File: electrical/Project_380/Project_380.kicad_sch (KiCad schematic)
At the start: 6 parts, among them J14 UART_to_USB, SW1 SW_SPST, U2 ESP32-WROOM

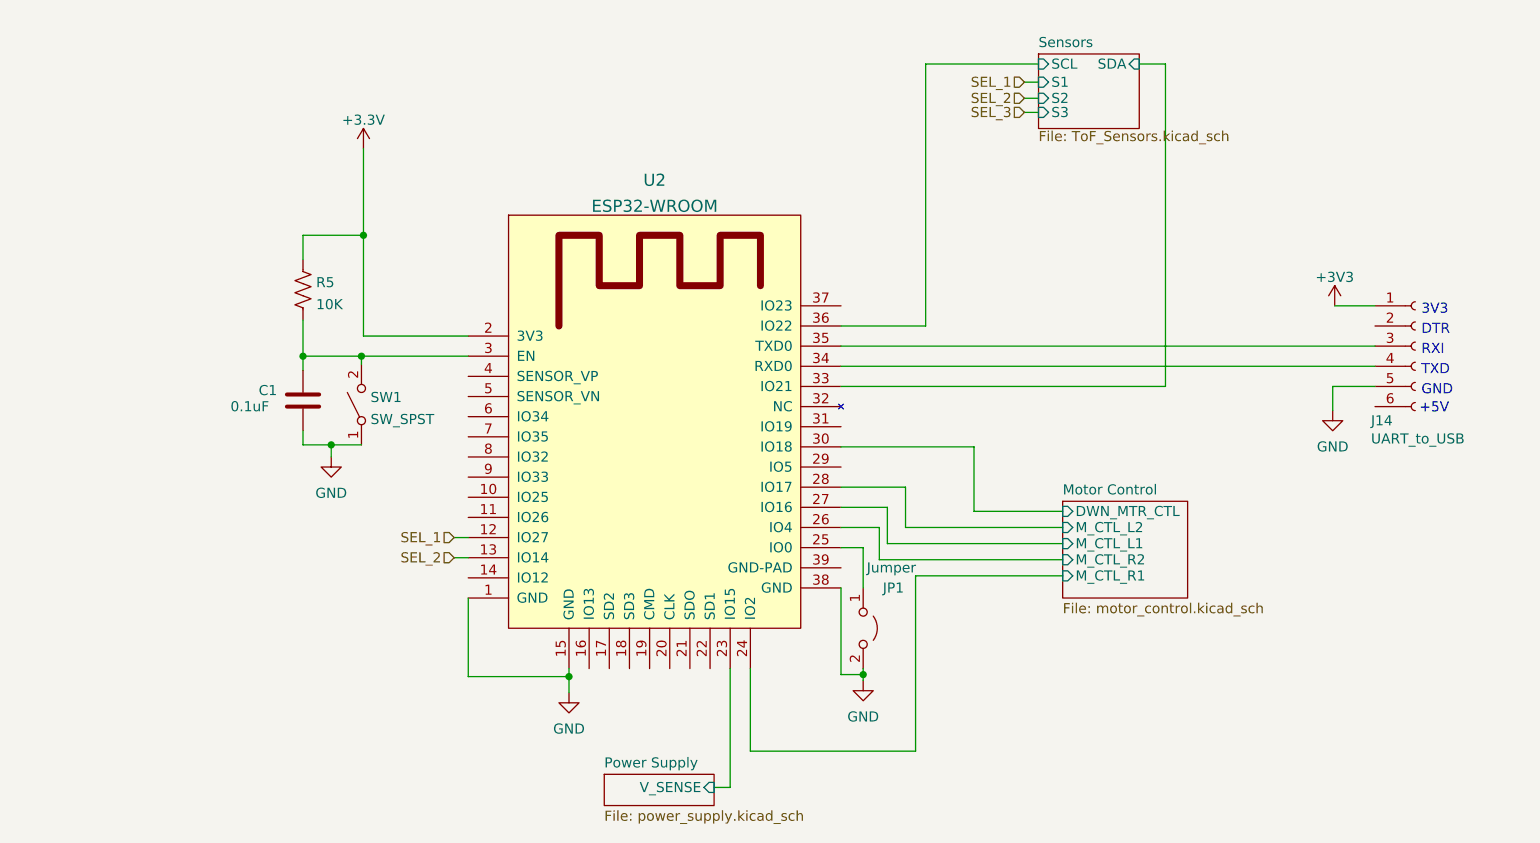
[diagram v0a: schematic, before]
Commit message: Make fixes to board, add silkscreen, and generate gerbers
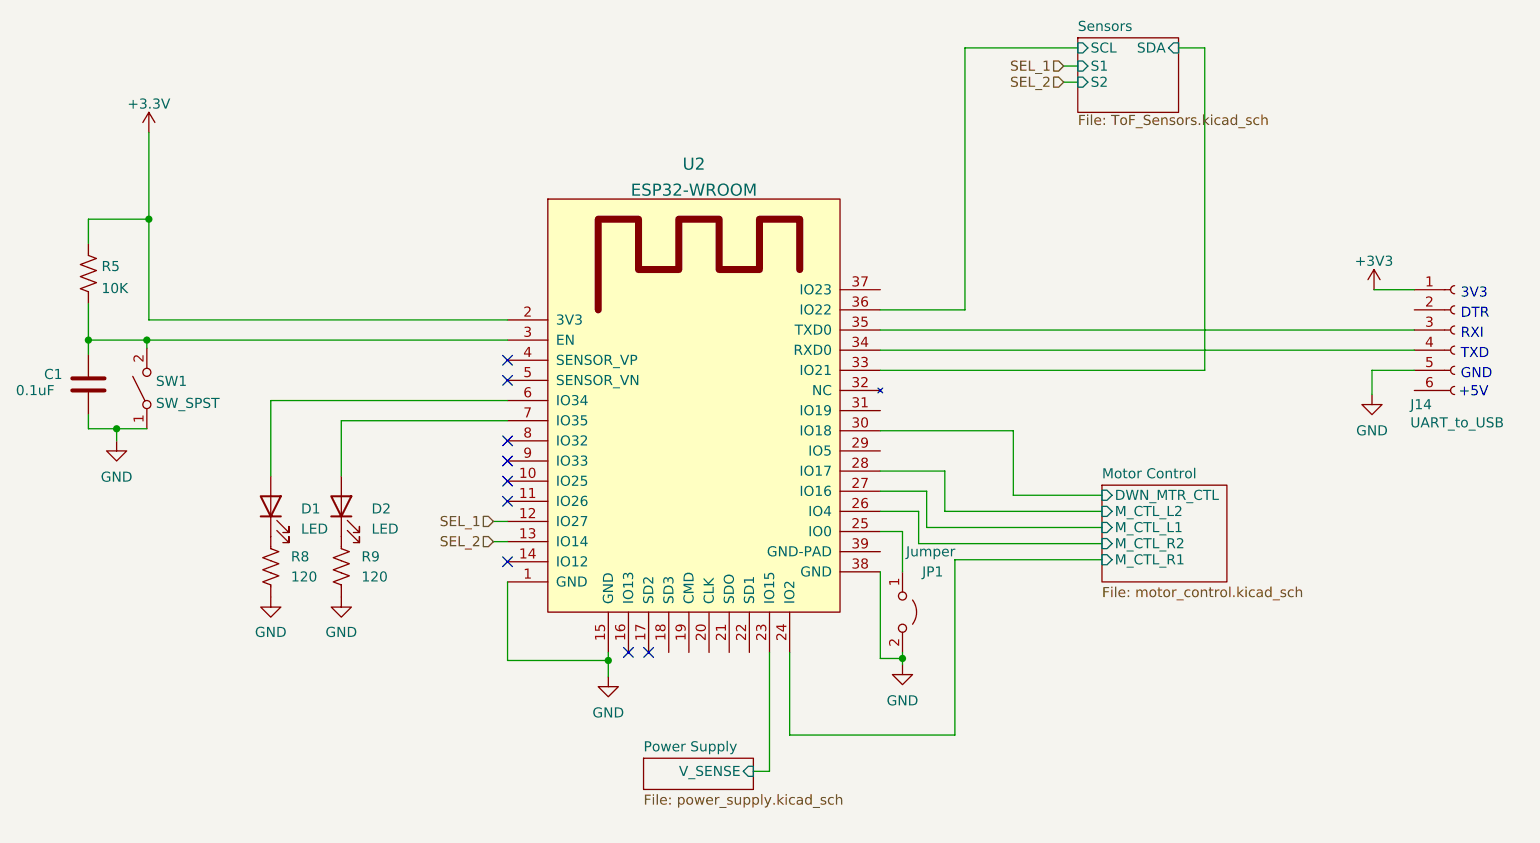
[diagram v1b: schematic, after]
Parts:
- added D1, D2: LED, LED_SMD:LED_1206_3216Metric_Pad1.42x1.75mm_HandSolder, symbol Device:LED
- added R8, R9: 120, Resistor_SMD:R_0805_2012Metric_Pad1.20x1.40mm_HandSolder, symbol Device:R_US
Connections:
- net GND: now also R8.2, R9.2
- net at U2.6 (IO34): now also D1.2 (A)
- net at U2.7 (IO35): now also D2.2 (A)
- new net: D1.1 (K), R8.1
- new net: D2.1 (K), R9.1
- no-connect marks 0 -> 9
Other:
- sheet Sensors ports: added none; removed S3
- moved on the sheet: C1, J14, JP1, R5, SW1, U2
